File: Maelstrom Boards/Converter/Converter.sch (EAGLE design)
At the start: 38 parts, among them Q1 BSS295, Q2 BSS295, Q3 BSS295

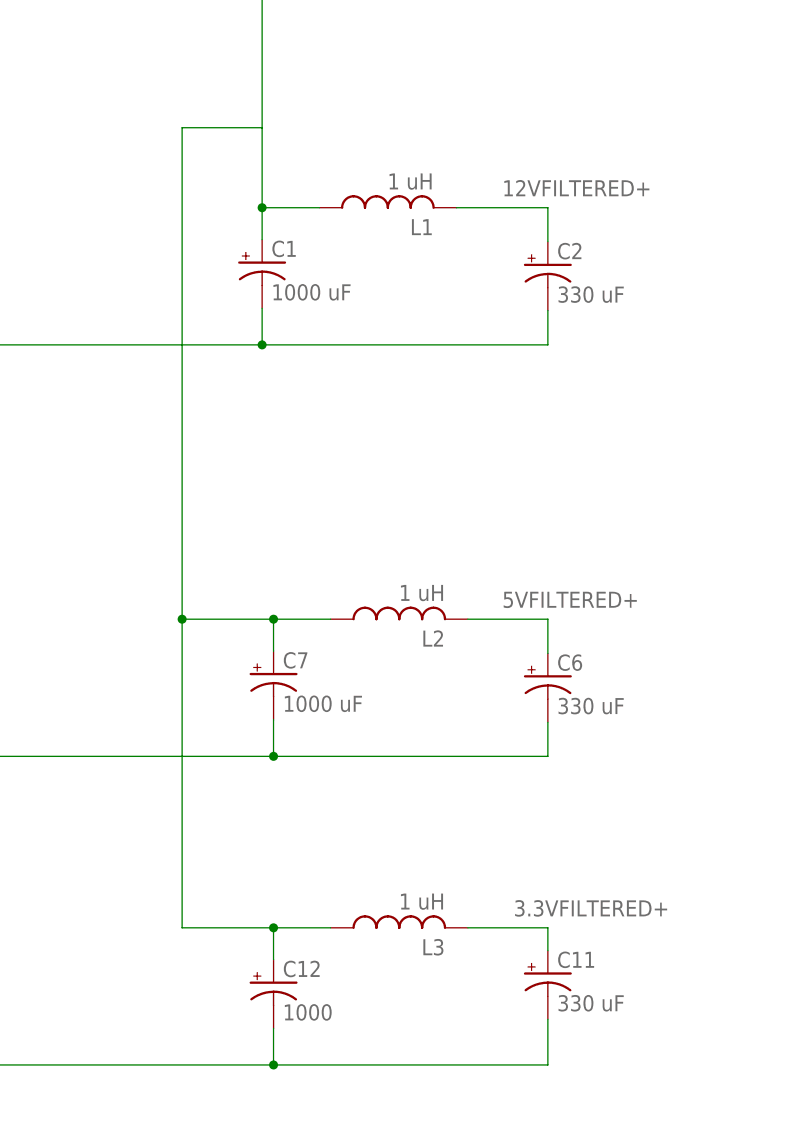
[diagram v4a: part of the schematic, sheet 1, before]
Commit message: Changing converter board parts
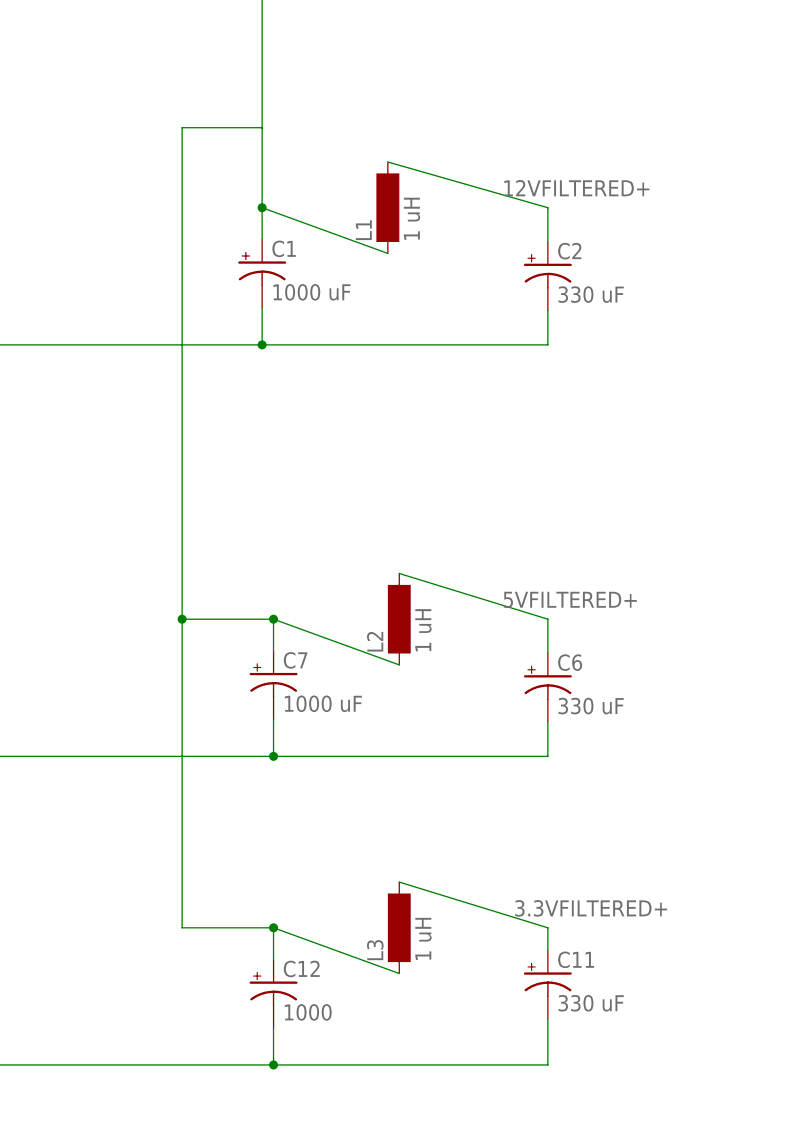
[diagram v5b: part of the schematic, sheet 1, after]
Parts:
- C1, C12, C7: device rcl:CPOL-USE3.5-10 -> rcl:CPOL-USE5-13
- C11, C2, C6: device rcl:CPOL-USE3.5-8 -> rcl:CPOL-USE5-10.5
- L1, L2, L3: device rcl:L-USWE-TPC -> inductor-neosid:MS85
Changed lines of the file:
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@@
 <part name="JETSON" library="con-molex-mini-fit" deviceset="39-30-?02?" device=""/>
 <part name="DIAMOND" library="con-molex-micro-fit" deviceset="43045-08" device=""/>
-<part name="L1" library="rcl" library_urn="urn:adsk.eagle:library:334" deviceset="L-US" device="WE-TPC" package3d_urn="urn:adsk.eagle:package:23507/1" value="1 uH"/>
-<part name="C1" library="rcl" library_urn="urn:adsk.eagle:library:334" deviceset="CPOL-US" device="E3.5-10" package3d_urn="urn:adsk.eagle:package:23351/1" value="1000 uF"/>
+<part name="L1" library="inductor-neosid" library_urn="urn:adsk.eagle:library:241" deviceset="MS85" device="" package3d_urn="urn:adsk.eagle:package:14698/1" value="1 uH"/>
+<part name="C1" library="rcl" library_urn="urn:adsk.eagle:library:334" deviceset="CPOL-US" device="E5-13" package3d_urn="urn:adsk.eagle:package:23375/1" value="1000 uF"/>
 <part name="C3" library="resistor" library_urn="urn:adsk.eagle:library:348" deviceset="C-US" device="C1206K" package3d_urn="urn:adsk.eagle:package:26202/1" value="47 uF"/>
 <part name="C4" library="resistor" library_urn="urn:adsk.eagle:library:348" deviceset="C-US" device="C1206K" package3d_urn="urn:adsk.eagle:package:26202/1" value="47 uF"/>
 <part name="C5" library="resistor" library_urn="urn:adsk.eagle:library:348" deviceset="C-US" device="C1206K" package3d_urn="urn:adsk.eagle:package:26202/1" value="47 uF"/>
-<part name="L2" library="rcl" library_urn="urn:adsk.eagle:library:334" deviceset="L-US" device="WE-TPC" package3d_urn="urn:adsk.eagle:package:23507/1" value="1 uH"/>
-<part name="C7" library="rcl" library_urn="urn:adsk.eagle:library:334" deviceset="CPOL-US" device="E3.5-10" package3d_urn="urn:adsk.eagle:package:23351/1" value="1000 uF"/>
+<part name="L2" library="inductor-neosid" library_urn="urn:adsk.eagle:library:241" deviceset="MS85" device="" package3d_urn="urn:adsk.eagle:package:14698/1" value="1 uH"/>
+<part name="C7" library="rcl" library_urn="urn:adsk.eagle:library:334" deviceset="CPOL-US" device="E5-13" package3d_urn="urn:adsk.eagle:package:23375/1" value="1000 uF"/>
 <part name="C8" library="resistor" library_urn="urn:adsk.eagle:library:348" deviceset="C-US" device="C1206K" package3d_urn="urn:adsk.eagle:package:26202/1" value="47 uF"/>
 <part name="C9" library="resistor" library_urn="urn:adsk.eagle:library:348" deviceset="C-US" device="C1206K" package3d_urn="urn:adsk.eagle:package:26202/1" value="47 uF"/>
 <part name="C10" library="resistor" library_urn="urn:adsk.eagle:library:348" deviceset="C-US" device="C1206K" package3d_urn="urn:adsk.eagle:package:26202/1" value="47 uF"/>
-<part name="L3" library="rcl" library_urn="urn:adsk.eagle:library:334" deviceset="L-US" device="WE-TPC" package3d_urn="urn:adsk.eagle:package:23507/1" value="1 uH"/>
-<part name="C12" library="rcl" library_urn="urn:adsk.eagle:library:334" deviceset="CPOL-US" device="E3.5-10" package3d_urn="urn:adsk.eagle:package:23351/1" value="1000"/>
+<part name="L3" library="inductor-neosid" library_urn="urn:adsk.eagle:library:241" deviceset="MS85" device="" package3d_urn="urn:adsk.eagle:package:14698/1" value="1 uH"/>
+<part name="C12" library="rcl" library_urn="urn:adsk.eagle:library:334" deviceset="CPOL-US" device="E5-13" package3d_urn="urn:adsk.eagle:package:23375/1" value="1000"/>
 <part name="C13" library="resistor" library_urn="urn:adsk.eagle:library:348" deviceset="C-US" device="C1206K" package3d_urn="urn:adsk.eagle:package:26202/1" value="47 uF"/>
 <part name="C14" library="resistor" library_urn="urn:adsk.eagle:library:348" deviceset="C-US" device="C1206K" package3d_urn="urn:adsk.eagle:package:26202/1" value="47 uF"/>
@@
 <part name="P+3" library="supply1" library_urn="urn:adsk.eagle:library:371" deviceset="+5V" device=""/>
 <part name="AGND7" library="supply1" library_urn="urn:adsk.eagle:library:371" deviceset="AGND" device=""/>
-<part name="C2" library="rcl" library_urn="urn:adsk.eagle:library:334" deviceset="CPOL-US" device="E3.5-8" package3d_urn="urn:adsk.eagle:package:23360/2" value="330 uF"/>
-<part name="C6" library="rcl" library_urn="urn:adsk.eagle:library:334" deviceset="CPOL-US" device="E3.5-8" package3d_urn="urn:adsk.eagle:package:23360/2" value="330 uF"/>
-<part name="C11" library="rcl" library_urn="urn:adsk.eagle:library:334" deviceset="CPOL-US" device="E3.5-8" package3d_urn="urn:adsk.eagle:package:23360/2" value="330 uF"/>
+<part name="C2" library="rcl" library_urn="urn:adsk.eagle:library:334" deviceset="CPOL-US" device="E5-10.5" package3d_urn="urn:adsk.eagle:package:23372/1" value="330 uF"/>
+<part name="C6" library="rcl" library_urn="urn:adsk.eagle:library:334" deviceset="CPOL-US" device="E5-10.5" package3d_urn="urn:adsk.eagle:package:23372/1" value="330 uF"/>
+<part name="C11" library="rcl" library_urn="urn:adsk.eagle:library:334" deviceset="CPOL-US" device="E5-10.5" package3d_urn="urn:adsk.eagle:package:23372/1" value="330 uF"/>
 <part name="P+4" library="supply1" library_urn="urn:adsk.eagle:library:371" deviceset="V+" device=""/>
 <part name="R1" library="rcl" library_urn="urn:adsk.eagle:library:334" deviceset="R-US_" device="R0603" package3d_urn="urn:adsk.eagle:package:23555/2" value="10K"/>
@@
 <segment>
 <pinref part="L1" gate="G$1" pin="2"/>
-<wire x1="40.64" y1="191.77" x2="30.48" y2="191.77" width="0.1524" layer="91"/>
+<wire x1="40.64" y1="191.77" x2="22.86" y2="196.85" width="0.1524" layer="91"/>
 <pinref part="C2" gate="G$1" pin="+"/>
 <wire x1="40.64" y1="191.77" x2="40.64" y2="187.96" width="0.1524" layer="91"/>
@@
 <segment>
 <pinref part="L2" gate="G$1" pin="2"/>
-<wire x1="40.64" y1="146.05" x2="31.75" y2="146.05" width="0.1524" layer="91"/>
+<wire x1="40.64" y1="146.05" x2="24.13" y2="151.13" width="0.1524" layer="91"/>
 <pinref part="C6" gate="G$1" pin="+"/>
 <wire x1="40.64" y1="146.05" x2="40.64" y2="142.24" width="0.1524" layer="91"/>
@@
 <segment>
 <pinref part="L3" gate="G$1" pin="2"/>
-<wire x1="40.64" y1="111.76" x2="31.75" y2="111.76" width="0.1524" layer="91"/>
+<wire x1="40.64" y1="111.76" x2="24.13" y2="116.84" width="0.1524" layer="91"/>
 <pinref part="C11" gate="G$1" pin="+"/>
 <wire x1="40.64" y1="111.76" x2="40.64" y2="109.22" width="0.1524" layer="91"/>
@@
 <wire x1="-16.51" y1="262.89" x2="8.89" y2="262.89" width="0.1524" layer="91"/>
 <pinref part="L1" gate="G$1" pin="1"/>
-<wire x1="15.24" y1="191.77" x2="8.89" y2="191.77" width="0.1524" layer="91"/>
+<wire x1="22.86" y1="186.69" x2="8.89" y2="191.77" width="0.1524" layer="91"/>
 <wire x1="8.89" y1="262.89" x2="8.89" y2="200.66" width="0.1524" layer="91"/>
 <pinref part="BALANCEDRAWIN" gate="G$1" pin="2"/>
@@
 <wire x1="0" y1="200.66" x2="0" y2="146.05" width="0.1524" layer="91"/>
 <pinref part="L2" gate="G$1" pin="1"/>
-<wire x1="16.51" y1="146.05" x2="10.16" y2="146.05" width="0.1524" layer="91"/>
+<wire x1="24.13" y1="140.97" x2="10.16" y2="146.05" width="0.1524" layer="91"/>
 <pinref part="C7" gate="G$1" pin="+"/>
 <wire x1="10.16" y1="146.05" x2="10.16" y2="142.494" width="0.1524" layer="91"/>
@@
 <junction x="10.16" y="146.05"/>
 <pinref part="L3" gate="G$1" pin="1"/>
-<wire x1="16.51" y1="111.76" x2="10.16" y2="111.76" width="0.1524" layer="91"/>
+<wire x1="24.13" y1="106.68" x2="10.16" y2="111.76" width="0.1524" layer="91"/>
 <pinref part="C12" gate="G$1" pin="+"/>
 <wire x1="10.16" y1="111.76" x2="10.16" y2="108.204" width="0.1524" layer="91"/>
@@
 packages will not be understood (or retained) with this version.
 </note>
+<note version="8.4" severity="warning">
+Since Version 8.4, EAGLE supports properties for SPICE simulation.
+Probes in schematics and SPICE mapping objects found in parts and library devices
+will not be understood with this version. Update EAGLE to the latest version
+for full support of SPICE simulation.
+</note>
 </compatibility>

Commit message: Changed values
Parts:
- R1, R3, R8: value 10K -> 100K
- R2, R7, R9: value 1.35K -> 13K
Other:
- moved on the sheet: L1, L2, L3
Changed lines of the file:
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@@
 <part name="C11" library="rcl" library_urn="urn:adsk.eagle:library:334" deviceset="CPOL-US" device="E5-10.5" package3d_urn="urn:adsk.eagle:package:23372/1" value="330 uF"/>
 <part name="P+4" library="supply1" library_urn="urn:adsk.eagle:library:371" deviceset="V+" device=""/>
-<part name="R1" library="rcl" library_urn="urn:adsk.eagle:library:334" deviceset="R-US_" device="R0603" package3d_urn="urn:adsk.eagle:package:23555/2" value="10K"/>
-<part name="R2" library="rcl" library_urn="urn:adsk.eagle:library:334" deviceset="R-US_" device="R0603" package3d_urn="urn:adsk.eagle:package:23555/2" value="1.35K"/>
+<part name="R1" library="rcl" library_urn="urn:adsk.eagle:library:334" deviceset="R-US_" device="R0603" package3d_urn="urn:adsk.eagle:package:23555/2" value="100K"/>
+<part name="R2" library="rcl" library_urn="urn:adsk.eagle:library:334" deviceset="R-US_" device="R0603" package3d_urn="urn:adsk.eagle:package:23555/2" value="13K"/>
 <part name="P+5" library="supply1" library_urn="urn:adsk.eagle:library:371" deviceset="V+" device=""/>
-<part name="R3" library="rcl" library_urn="urn:adsk.eagle:library:334" deviceset="R-US_" device="R0603" package3d_urn="urn:adsk.eagle:package:23555/2" value="10K"/>
-<part name="R7" library="rcl" library_urn="urn:adsk.eagle:library:334" deviceset="R-US_" device="R0603" package3d_urn="urn:adsk.eagle:package:23555/2" value="1.35K"/>
+<part name="R3" library="rcl" library_urn="urn:adsk.eagle:library:334" deviceset="R-US_" device="R0603" package3d_urn="urn:adsk.eagle:package:23555/2" value="100K"/>
+<part name="R7" library="rcl" library_urn="urn:adsk.eagle:library:334" deviceset="R-US_" device="R0603" package3d_urn="urn:adsk.eagle:package:23555/2" value="13K"/>
 <part name="P+6" library="supply1" library_urn="urn:adsk.eagle:library:371" deviceset="V+" device=""/>
-<part name="R8" library="rcl" library_urn="urn:adsk.eagle:library:334" deviceset="R-US_" device="R0603" package3d_urn="urn:adsk.eagle:package:23555/2" value="10K"/>
-<part name="R9" library="rcl" library_urn="urn:adsk.eagle:library:334" deviceset="R-US_" device="R0603" package3d_urn="urn:adsk.eagle:package:23555/2" value="1.35K"/>
+<part name="R8" library="rcl" library_urn="urn:adsk.eagle:library:334" deviceset="R-US_" device="R0603" package3d_urn="urn:adsk.eagle:package:23555/2" value="100K"/>
+<part name="R9" library="rcl" library_urn="urn:adsk.eagle:library:334" deviceset="R-US_" device="R0603" package3d_urn="urn:adsk.eagle:package:23555/2" value="13K"/>
 <part name="P+7" library="supply1" library_urn="urn:adsk.eagle:library:371" deviceset="V+" device=""/>
 <part name="AGND8" library="supply1" library_urn="urn:adsk.eagle:library:371" deviceset="AGND" device=""/>
@@
 <instance part="JETSON" gate="G$1" x="209.55" y="256.54" rot="R90"/>
 <instance part="DIAMOND" gate="G$1" x="227.33" y="256.54" rot="R90"/>
-<instance part="L1" gate="G$1" x="22.86" y="191.77" rot="R90"/>
+<instance part="L1" gate="G$1" x="22.86" y="191.77"/>
 <instance part="C1" gate="G$1" x="8.89" y="185.674"/>
 <instance part="C3" gate="G$1" x="144.78" y="185.42"/>
 <instance part="C4" gate="G$1" x="158.75" y="185.42"/>
 <instance part="C5" gate="G$1" x="171.45" y="185.42"/>
-<instance part="L2" gate="G$1" x="24.13" y="146.05" rot="R90"/>
+<instance part="L2" gate="G$1" x="24.13" y="146.05"/>
 <instance part="C7" gate="G$1" x="10.16" y="139.954"/>
 <instance part="C8" gate="G$1" x="146.05" y="139.7"/>
 <instance part="C9" gate="G$1" x="160.02" y="139.7"/>
 <instance part="C10" gate="G$1" x="172.72" y="139.7"/>
-<instance part="L3" gate="G$1" x="24.13" y="111.76" rot="R90"/>
+<instance part="L3" gate="G$1" x="24.13" y="111.76"/>
 <instance part="C12" gate="G$1" x="10.16" y="105.664"/>
 <instance part="C13" gate="G$1" x="146.05" y="105.41"/>
@@
 <segment>
 <pinref part="L1" gate="G$1" pin="2"/>
-<wire x1="40.64" y1="191.77" x2="22.86" y2="196.85" width="0.1524" layer="91"/>
+<wire x1="40.64" y1="191.77" x2="27.94" y2="191.77" width="0.1524" layer="91"/>
 <pinref part="C2" gate="G$1" pin="+"/>
 <wire x1="40.64" y1="191.77" x2="40.64" y2="187.96" width="0.1524" layer="91"/>
@@
 <segment>
 <pinref part="L2" gate="G$1" pin="2"/>
-<wire x1="40.64" y1="146.05" x2="24.13" y2="151.13" width="0.1524" layer="91"/>
+<wire x1="40.64" y1="146.05" x2="29.21" y2="146.05" width="0.1524" layer="91"/>
 <pinref part="C6" gate="G$1" pin="+"/>
 <wire x1="40.64" y1="146.05" x2="40.64" y2="142.24" width="0.1524" layer="91"/>
@@
 <segment>
 <pinref part="L3" gate="G$1" pin="2"/>
-<wire x1="40.64" y1="111.76" x2="24.13" y2="116.84" width="0.1524" layer="91"/>
+<wire x1="40.64" y1="111.76" x2="29.21" y2="111.76" width="0.1524" layer="91"/>
 <pinref part="C11" gate="G$1" pin="+"/>
 <wire x1="40.64" y1="111.76" x2="40.64" y2="109.22" width="0.1524" layer="91"/>
@@
 <wire x1="-16.51" y1="262.89" x2="8.89" y2="262.89" width="0.1524" layer="91"/>
 <pinref part="L1" gate="G$1" pin="1"/>
-<wire x1="22.86" y1="186.69" x2="8.89" y2="191.77" width="0.1524" layer="91"/>
+<wire x1="17.78" y1="191.77" x2="8.89" y2="191.77" width="0.1524" layer="91"/>
 <wire x1="8.89" y1="262.89" x2="8.89" y2="200.66" width="0.1524" layer="91"/>
 <pinref part="BALANCEDRAWIN" gate="G$1" pin="2"/>
@@
 <wire x1="0" y1="200.66" x2="0" y2="146.05" width="0.1524" layer="91"/>
 <pinref part="L2" gate="G$1" pin="1"/>
-<wire x1="24.13" y1="140.97" x2="10.16" y2="146.05" width="0.1524" layer="91"/>
+<wire x1="19.05" y1="146.05" x2="10.16" y2="146.05" width="0.1524" layer="91"/>
 <pinref part="C7" gate="G$1" pin="+"/>
 <wire x1="10.16" y1="146.05" x2="10.16" y2="142.494" width="0.1524" layer="91"/>
@@
 <junction x="10.16" y="146.05"/>
 <pinref part="L3" gate="G$1" pin="1"/>
-<wire x1="24.13" y1="106.68" x2="10.16" y2="111.76" width="0.1524" layer="91"/>
+<wire x1="19.05" y1="111.76" x2="10.16" y2="111.76" width="0.1524" layer="91"/>
 <pinref part="C12" gate="G$1" pin="+"/>
 <wire x1="10.16" y1="111.76" x2="10.16" y2="108.204" width="0.1524" layer="91"/>

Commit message: New schematic template and converter fixes
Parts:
- removed BALANCEDRAWIN: 39-30-06, con-molex-mini-fit:39-30-06
- removed DIAMOND: 43045-08, con-molex-micro-fit:43045-08
- removed JETSON, PNUEMATICS: 39-30-02, con-molex-mini-fit:39-30-02
- added 12V_OUT, BALANCDIN, MOBO: 39-30-06, con-molex-mini-fit:39-30-06
- C11, C6: value 330 uF -> 1000 uF; device rcl:CPOL-USE5-10.5 -> rcl:CPOL-USE5-13
- C12: value 1000 -> 330 uF; device rcl:CPOL-USE5-13 -> rcl:CPOL-USE5-10.5
- C7: value 1000 uF -> 330 uF; device rcl:CPOL-USE5-13 -> rcl:CPOL-USE5-10.5
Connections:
- net 12VTRIM renamed N$1
- net 3.3VTRIM renamed N$3
- net 5VTRIM renamed N$2
- removed net 12VFILTERED+: 12VCONVERTER.1,VIN(+), C2.+, L1.2
- removed net 3.3VFILTERED+: 3.3VCONVERTER.1,VIN(+), C11.+, L3.2
- removed net 5VFILTERED+: 5VCONVERTER.1,VIN(+), C6.+, L2.2
- removed net BALANCED+: BALANCEDRAWIN.1, BALANCEDRAWIN.2, BALANCEDRAWIN.3, C1.+, C12.+, C7.+, L1.1, L2.1, L3.1, R1.2, R3.2, R8.2
- new net 12VFILTERED: 12VCONVERTER.1,VIN(+), C12.+, L3.2
- new net 3.3VFILTERED: 3.3VCONVERTER.1,VIN(+), C7.+, L2.2
- new net 5VFILTERED: 5VCONVERTER.1,VIN(+), C2.+, L1.2
- new net V+: BALANCDIN.1, BALANCDIN.2, BALANCDIN.3, C1.+, C11.+, C6.+, L1.1, L2.1, L3.1, R1.2, R3.2, R8.2
- net +12V: now also 12V_OUT.1, 12V_OUT.2, 12V_OUT.3, MOBO.1, MOBO.2, MOBO.3; no longer DIAMOND.1, DIAMOND.2, DIAMOND.3, DIAMOND.4, JETSON.1, PNUEMATICS.1
- net AGND: now also 12V_OUT.4, 12V_OUT.5, 12V_OUT.6, BALANCDIN.4, BALANCDIN.5, BALANCDIN.6, MOBO.4, MOBO.5, MOBO.6; no longer BALANCEDRAWIN.4, BALANCEDRAWIN.5, BALANCEDRAWIN.6, DIAMOND.5, DIAMOND.6, DIAMOND.7, DIAMOND.8, JETSON.2, PNUEMATICS.2
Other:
- note added: "C:/Users/blain/Downloads/Black and White.bmp"
- note added: "Electrical Team"
- note added: "Underwater Robotics Team Ohio State University"
- moved on the sheet: C10, C13, C14, C15, C3, C4, C5, C8, C9, Q1, Q2, Q3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
